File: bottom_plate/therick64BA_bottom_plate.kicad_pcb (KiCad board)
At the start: 2 copper layers, 314.3 x 76.2 mm, 12 parts, among them U1 HOLE

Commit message: Update to 19mm
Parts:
- removed Ref**: Plate_hole_4mm, random-keyboard-parts:Plate_hole_4mm
- added U10: HOLE, Keeb_footprints:MX100_outline, F.Cu at (226.9, 44.5)
- added U11: HOLE, Keeb_footprints:MX100_outline, F.Cu at (245.9, 44.5)
- added U12: HOLE, Keeb_footprints:MX100_outline, F.Cu at (264.9, 44.5)
- added U13: HOLE, Keeb_footprints:MX100_outline, F.Cu at (55.9, 63.5)
- added U14: HOLE, Keeb_footprints:MX100_outline, F.Cu at (74.9, 63.5)
- added U15: HOLE, Keeb_footprints:MX100_outline, F.Cu at (93.9, 63.5)
- added U16: HOLE, Keeb_footprints:MX100_outline, F.Cu at (112.9, 63.5)
- added U17: HOLE, Keeb_footprints:MX100_outline, F.Cu at (131.9, 63.5)
- added U18: HOLE, Keeb_footprints:MX100_outline, F.Cu at (150.9, 63.5)
- added U19: HOLE, Keeb_footprints:MX100_outline, F.Cu at (169.9, 63.5)
- added U2: HOLE, Keeb_footprints:MX100_outline, F.Cu at (74.9, 44.5)
- added U20: HOLE, Keeb_footprints:MX100_outline, F.Cu at (188.9, 63.5)
- added U21: HOLE, Keeb_footprints:MX100_outline, F.Cu at (207.9, 63.5)
- added U22: HOLE, Keeb_footprints:MX100_outline, F.Cu at (226.9, 63.5)
- added U23: HOLE, Keeb_footprints:MX100_outline, F.Cu at (245.9, 63.5)
- added U24: HOLE, Keeb_footprints:MX100_outline, F.Cu at (264.9, 63.5)
- added U25: HOLE, Keeb_footprints:MX100_outline, F.Cu at (55.9, 82.5)
- added U26: HOLE, Keeb_footprints:MX100_outline, F.Cu at (74.9, 82.5)
- added U27: HOLE, Keeb_footprints:MX100_outline, F.Cu at (93.9, 82.5)
- added U28: HOLE, Keeb_footprints:MX100_outline, F.Cu at (112.9, 82.5)
- added U29: HOLE, Keeb_footprints:MX100_outline, F.Cu at (131.9, 82.5)
- added U3: HOLE, Keeb_footprints:MX100_outline, F.Cu at (93.9, 44.5)
- added U30: HOLE, Keeb_footprints:MX100_outline, F.Cu at (150.9, 82.5)
- added U31: HOLE, Keeb_footprints:MX100_outline, F.Cu at (169.9, 82.5)
- added U32: HOLE, Keeb_footprints:MX100_outline, F.Cu at (188.9, 82.5)
- added U33: HOLE, Keeb_footprints:MX100_outline, F.Cu at (207.9, 82.5)
- added U34: HOLE, Keeb_footprints:MX100_outline, F.Cu at (226.9, 82.5)
- added U35: HOLE, Keeb_footprints:MX100_outline, F.Cu at (245.9, 82.5)
- added U36: HOLE, Keeb_footprints:MX100_outline, F.Cu at (264.9, 82.5)
- added U37: HOLE, Keeb_footprints:MX100_outline, F.Cu at (55.9, 101.5)
- added U38: HOLE, Keeb_footprints:MX100_outline, F.Cu at (74.9, 101.5)
- added U39: HOLE, Keeb_footprints:MX100_outline, F.Cu at (93.9, 101.5)
- added U4: HOLE, Keeb_footprints:MX100_outline, F.Cu at (112.9, 44.5)
- added U40: HOLE, Keeb_footprints:MX100_outline, F.Cu at (112.9, 101.5)
- added U41: HOLE, Keeb_footprints:MX100_outline, F.Cu at (131.9, 101.5)
- added U42: HOLE, Keeb_footprints:MX100_outline, F.Cu at (150.9, 101.5)
- added U43: HOLE, Keeb_footprints:MX100_outline, F.Cu at (169.9, 101.5)
- added U44: HOLE, Keeb_footprints:MX100_outline, F.Cu at (188.9, 101.5)
- added U45: HOLE, Keeb_footprints:MX100_outline, F.Cu at (207.9, 101.5)
- added U46: HOLE, Keeb_footprints:MX100_outline, F.Cu at (226.9, 101.5)
- added U47: HOLE, Keeb_footprints:MX100_outline, F.Cu at (245.9, 101.5)
- added U48: HOLE, Keeb_footprints:MX100_outline, F.Cu at (264.9, 101.5)
- added U49: HOLE, Keeb_footprints:MX100_outline, F.Cu at (293.7, 44.5)
- added U5: HOLE, Keeb_footprints:MX100_outline, F.Cu at (131.9, 44.5)
- added U50: HOLE, Keeb_footprints:MX100_outline, F.Cu at (312.7, 44.5)
- added U51: HOLE, Keeb_footprints:MX100_outline, F.Cu at (331.7, 44.5)
- added U52: HOLE, Keeb_footprints:MX100_outline, F.Cu at (350.7, 44.5)
- added U53: HOLE, Keeb_footprints:MX100_outline, F.Cu at (293.7, 63.5)
- added U54: HOLE, Keeb_footprints:MX100_outline, F.Cu at (312.7, 63.5)
- added U55: HOLE, Keeb_footprints:MX100_outline, F.Cu at (331.7, 63.5)
- added U56: HOLE, Keeb_footprints:MX100_outline, F.Cu at (350.7, 63.5)
- added U57: HOLE, Keeb_footprints:MX100_outline, F.Cu at (293.7, 82.5)
- added U58: HOLE, Keeb_footprints:MX100_outline, F.Cu at (312.7, 82.5)
- added U59: HOLE, Keeb_footprints:MX100_outline, F.Cu at (331.7, 82.5)
- added U6: HOLE, Keeb_footprints:MX100_outline, F.Cu at (150.9, 44.5)
- added U60: HOLE, Keeb_footprints:MX100_outline, F.Cu at (350.7, 82.5)
- added U61: HOLE, Keeb_footprints:MX100_outline, F.Cu at (293.7, 101.5)
- added U62: HOLE, Keeb_footprints:MX100_outline, F.Cu at (312.7, 101.5)
- added U63: HOLE, Keeb_footprints:MX100_outline, F.Cu at (331.7, 101.5)
- added U64: HOLE, Keeb_footprints:MX100_outline, F.Cu at (350.7, 101.5)
- added U65: HOLE, Artwork:rick_large, B.Cu at (237.6, 76.6)
- added U66: HOLE, acheron_Hardware:MouseBite_IPC7351, F.Cu at (274.4, 101.5)
- added U67: HOLE, acheron_Hardware:MouseBite_IPC7351, F.Cu at (274.4, 87.0)
- added U68: HOLE, acheron_Hardware:MouseBite_IPC7351, F.Cu at (274.4, 73.0)
- added U69: HOLE, acheron_Hardware:MouseBite_IPC7351, F.Cu at (274.4, 58.9)
- added U7: HOLE, Keeb_footprints:MX100_outline, F.Cu at (169.9, 44.5)
- added U70: HOLE, acheron_Hardware:MouseBite_IPC7351, F.Cu at (274.4, 44.5)
- added U8: HOLE, Keeb_footprints:MX100_outline, F.Cu at (188.9, 44.5)
- added U9: HOLE, Keeb_footprints:MX100_outline, F.Cu at (207.9, 44.5)
- U1: footprint Artwork:rick_large -> Keeb_footprints:MX100_outline; moved to F.Cu
- moved U1 226.2 mm to (55.9, 44.5), turned to 0 degrees
- moved H8 53.8 mm to (303.2, 92.0)
- moved H10 38.1 mm to (341.2, 54.0)
- moved H9 38.0 mm to (341.2, 92.0)
- moved H4 1.61 mm to (217.4, 54.0)
- moved H1 0.29 mm to (65.4, 73.0)
- moved H6 0.24 mm to (255.4, 73.0)
- moved H3 0.21 mm to (103.4, 92.0)
- moved H2 0.17 mm to (103.4, 54.0)
- moved H5 0.17 mm to (217.4, 92.0)
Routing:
- added copper zone on B.Cu, net GND
- added copper zone on F.Cu, net GND
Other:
- board size 314.3 x 76.2 mm -> 313.9 x 76 mm
- net class Default: clearance 0.2 -> 0.13; via_dia 0.8 -> 0.5; via_drill 0.4 -> 0.25
- net class Thick added: clearance 0.13, trace_width 0.5, via_dia 0.8, via_drill 0.5
- rule trace_clearance: 0.2 -> 0.13
- rule trace_min: 0.2 -> 0.13
- rule via_min_drill: 0.3 -> 0.25
- rule via_min_size: 0.4 -> 0.5
- board text added: "therick"
- board text added: "therick64BA_19mm"
- board text removed: "therick64"

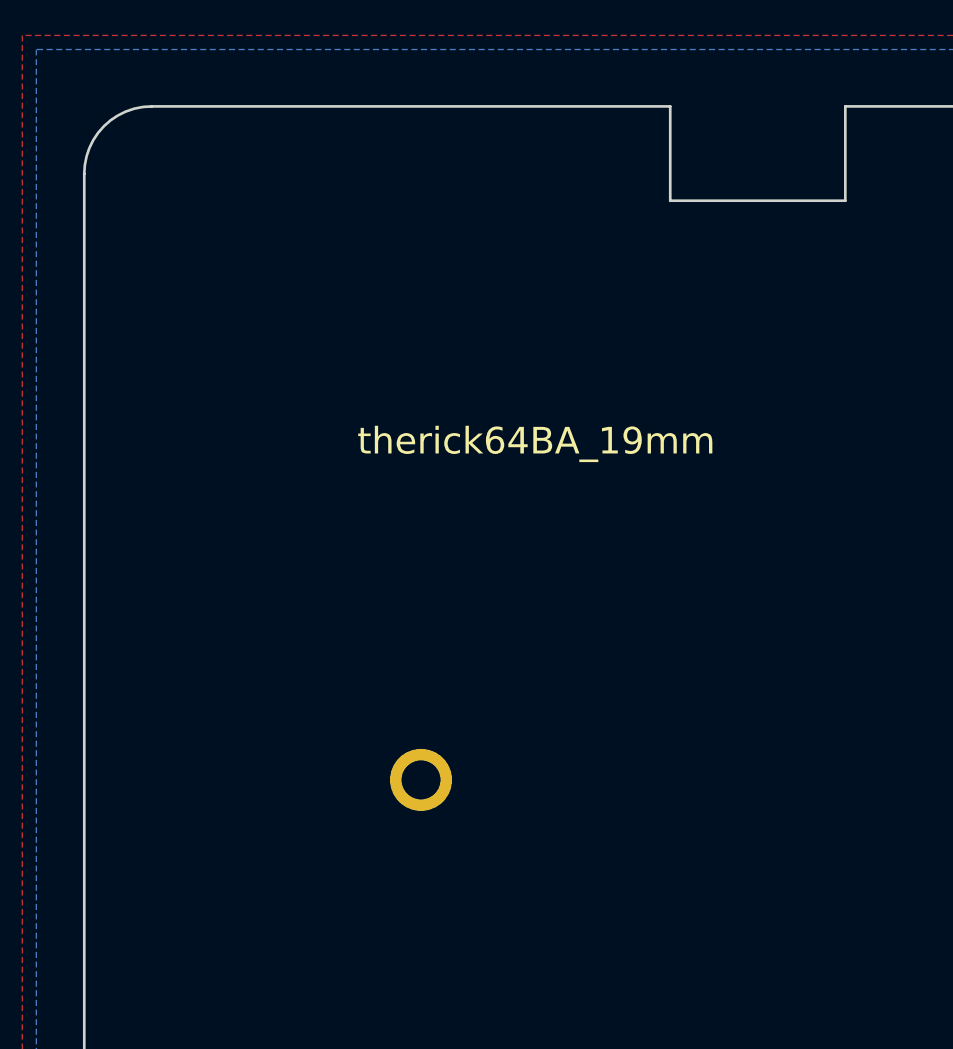
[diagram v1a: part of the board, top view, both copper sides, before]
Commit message: Changed pins to make routing cleaner
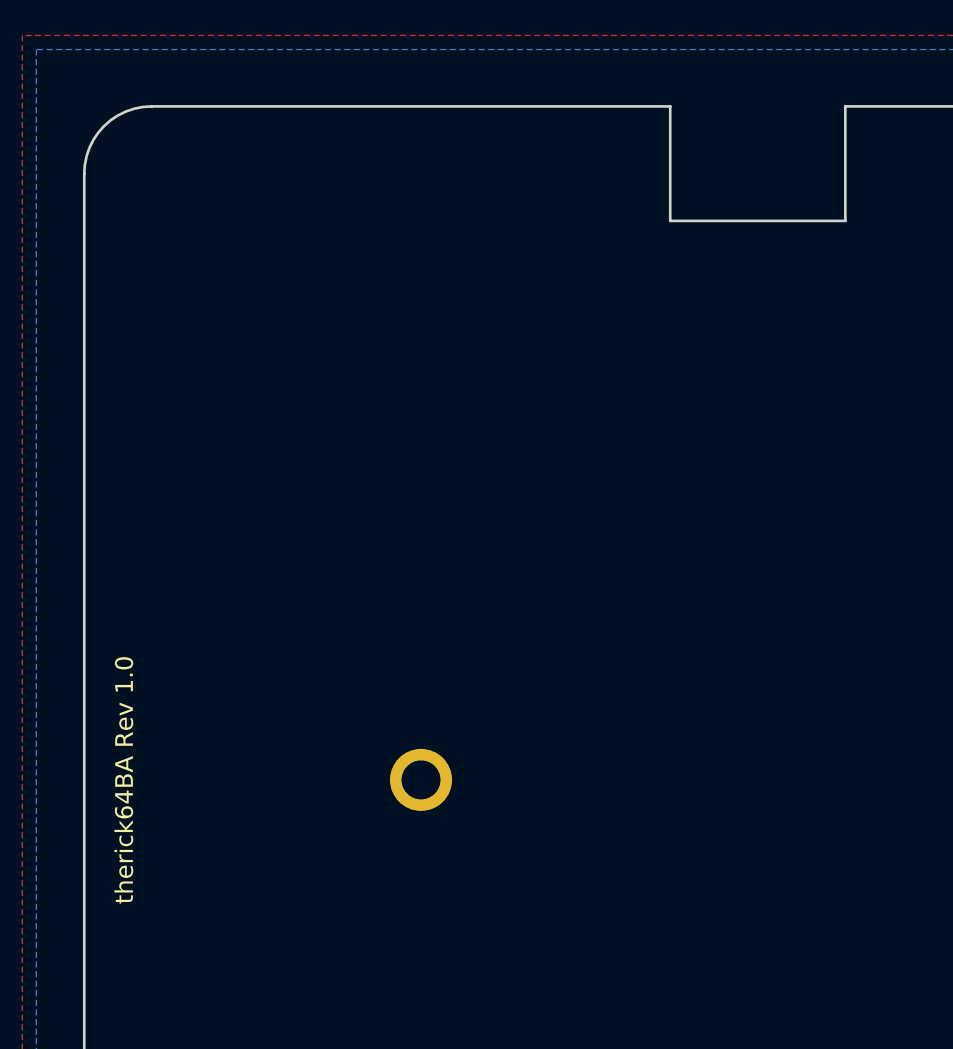
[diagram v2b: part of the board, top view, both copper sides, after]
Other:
- outline, holes or cut-outs redrawn
- board text added: "therick64BA Rev 1.0"
- board text removed: "therick"
- board text removed: "therick64BA_19mm"
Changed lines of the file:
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@@
   (general
     (thickness 1.6)
-    (drawings 69)
+    (drawings 68)
     (tracks 0)
     (zones 0)
@@
     (pad 1 thru_hole circle (at 0 0) (size 3.5 3.5) (drill 2.2) (layers *.Cu *.Mask))
   )
-  (gr_text therick64BA_19mm (at 61.760286 53.848) (layer F.SilkS)
-    (effects (font (size 1.5 1.5) (thickness 0.2)) (justify left))
+  (gr_text "therick64BA Rev 1.0" (at 48.639872 72.959808 90) (layer F.SilkS)
+    (effects (font (size 1 1) (thickness 0.15)))
   )
   (gr_arc (start 275.5 105.64) (end 276.64 105.64) (angle -180) (layer Edge.Cuts) (width 0.15))
@@
   (gr_arc (start 356.44 38.76) (end 360.24 38.76) (angle -90) (layer Edge.Cuts) (width 0.15))
   (gr_arc (start 356.44 107.16) (end 356.44 110.96) (angle -90) (layer Edge.Cuts) (width 0.15))
-  (gr_line (start 89.3 40.28) (end 89.3 34.96) (layer Edge.Cuts) (width 0.15))
-  (gr_line (start 79.42 40.28) (end 89.3 40.28) (layer Edge.Cuts) (width 0.15))
-  (gr_line (start 79.42 34.96) (end 79.42 40.28) (layer Edge.Cuts) (width 0.15))
+  (gr_line (start 89.3 41.419891) (end 89.3 34.96) (layer Edge.Cuts) (width 0.15))
+  (gr_line (start 79.419765 41.419891) (end 89.299765 41.419891) (layer Edge.Cuts) (width 0.15))
+  (gr_line (start 79.42 34.96) (end 79.419765 41.419891) (layer Edge.Cuts) (width 0.15))
   (gr_line (start 50.16 110.96) (end 270.56 110.96) (layer Edge.Cuts) (width 0.15))
   (gr_line (start 46.36 38.76) (end 46.36 107.16) (layer Edge.Cuts) (width 0.15))
@@
   (gr_line (start 101.6 53.975) (end 104.775 53.975) (layer Dwgs.User) (width 0.15))
   (gr_line (start 103.1875 55.5625) (end 103.1875 51.59375) (layer Dwgs.User) (width 0.15))
-  (gr_text therick (at 218.12 109.474) (layer B.SilkS)
-    (effects (font (size 1.5 1.5) (thickness 0.2)) (justify left mirror))
-  )
   (zone (net 1) (net_name GND) (layer F.Cu) (hatch edge 0.508)
     (connect_pads (clearance 0.508))
